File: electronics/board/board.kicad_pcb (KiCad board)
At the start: 2 copper layers, 141 x 30.5 mm, 80 parts, among them J1 Screw_Terminal_01x02, J10 Conn_01x02, J11 Conn_01x02, J12 Conn_01x02, J13 Conn_01x02, J14 Conn_01x02, J15 Conn_01x02, J16 Conn_01x02, J17 Conn_01x02, J18 Conn_01x02, J19 Conn_01x02, J2 Screw_Terminal_01x02, J20 Conn_01x02, J21 Conn_01x02, J22 Conn_01x02, J25 Screw_Terminal_01x01, J3 AVR-ISP-6, J4 USB_B_Micro, J5 Screw_Terminal_01x02, J6 Screw_Terminal_01x02, J7 Conn_01x02, J8 Conn_01x02, J9 Conn_01x02, Q1 IRF7404, SW1 SW_Push_Open_Dual, U1 LMV358, U2 ATmega32U4-AU, U3 NCP1117-5.0_TO252, U4 ST485EBDR, U5 ULN2803A, U6 ULN2803A, Y1 Crystal 16MHz

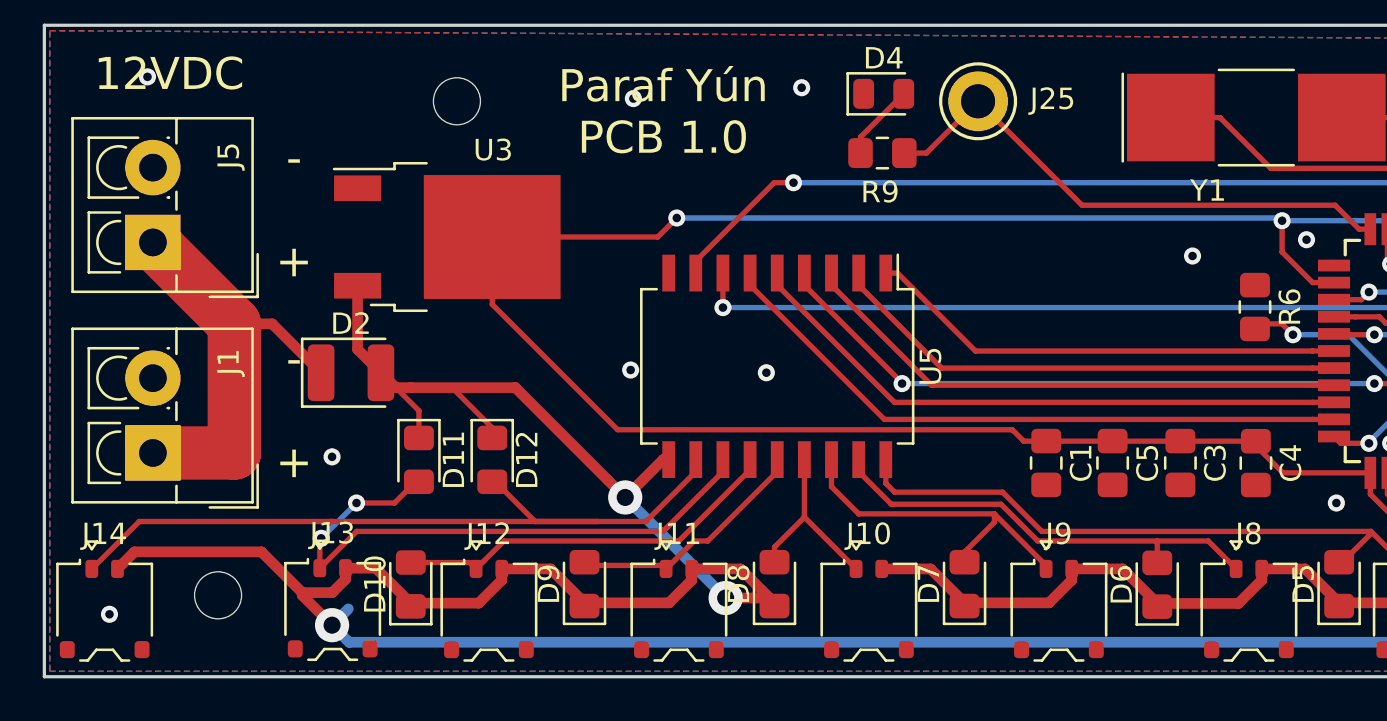
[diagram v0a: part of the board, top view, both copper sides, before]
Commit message: Diode protects only MCU
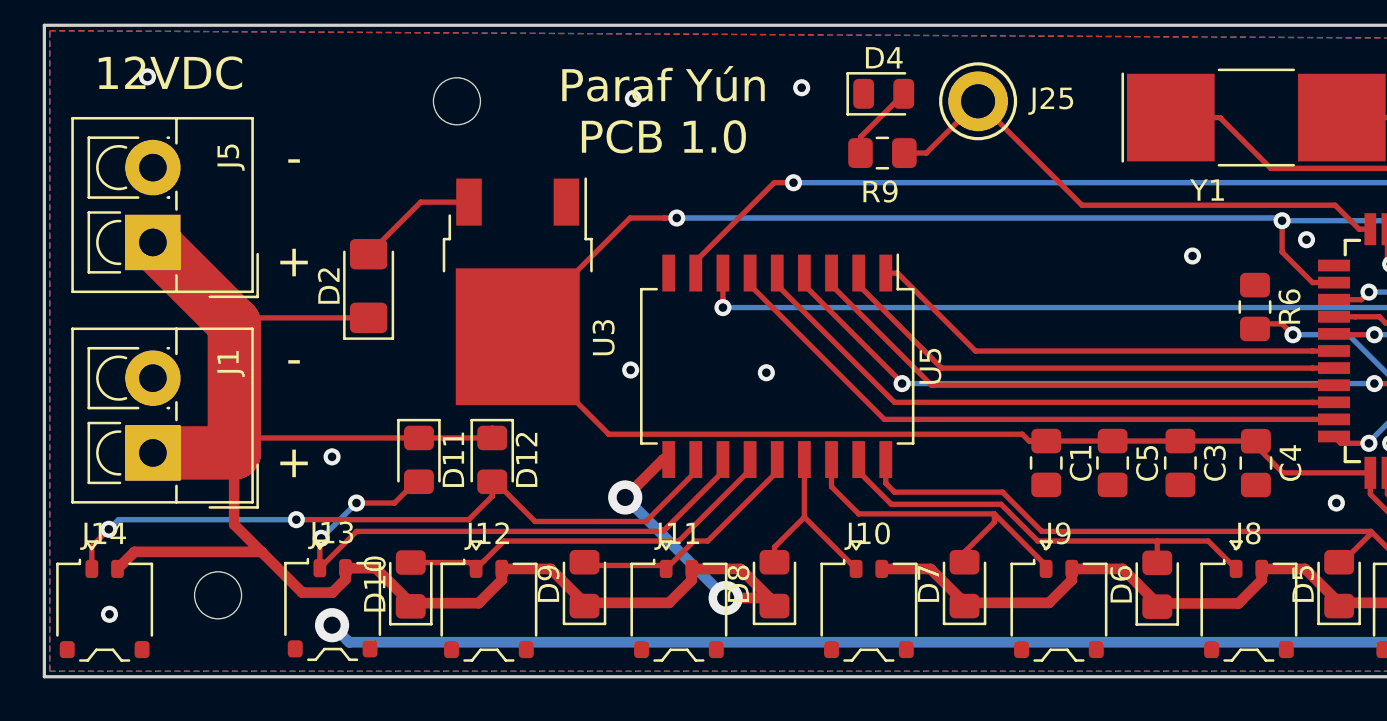
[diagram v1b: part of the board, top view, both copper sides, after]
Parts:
- D2: footprint Diode_SMD:D_1210_3225Metric -> Diode_SMD:D_1206_3216Metric_Pad1.42x1.75mm_HandSolder
- moved U3 4.18 mm to (86.9, 153.4), turned to 270 degrees
- moved D2 4.14 mm to (79.9, 153.2), turned to 90 degrees
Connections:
- D2 pad 1: Net-(D2-Pad1) -> +12V
- D2 pad 2: +12V -> Net-(D2-Pad2)
- J1 pad 1: Net-(D2-Pad1) -> +12V
- J5 pad 1: Net-(D2-Pad1) -> +12V
- U3 pad 3: +12V -> Net-(D2-Pad2)
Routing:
- net Net-(D2-Pad1): track 20.2 -> 0.00 mm
- net +12V: track 354.3 -> 363.3 mm
- net Net-(D2-Pad2): track 0.00 -> 5.71 mm
- net +5V: track 253.7 -> 249.8 mm
- net Net-(D12-Pad2): track 36.8 -> 33.5 mm, vias 0 -> 2

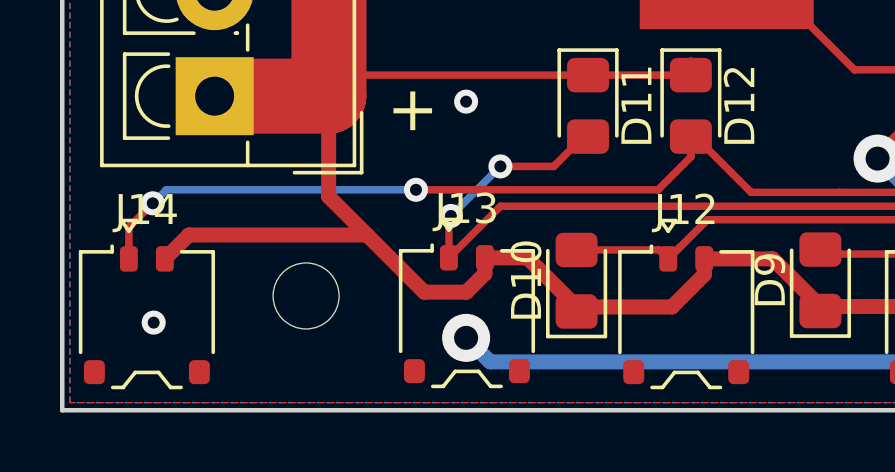
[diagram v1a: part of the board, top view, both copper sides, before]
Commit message: Bugfixes R 10k and 12v track
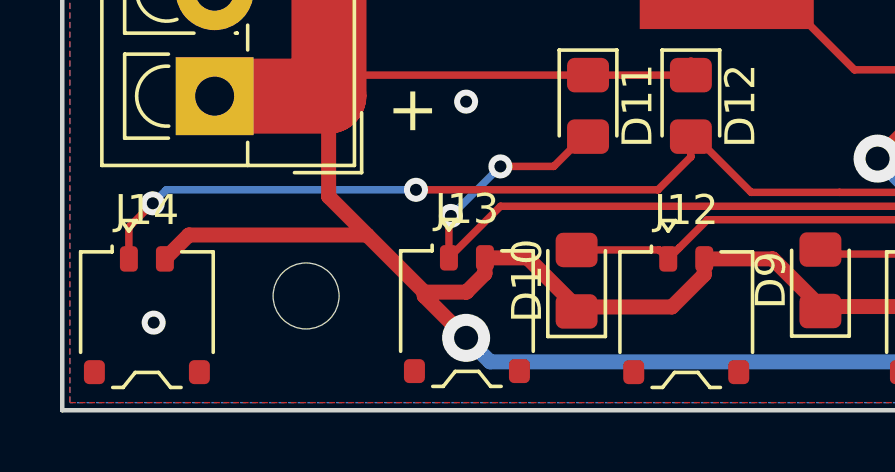
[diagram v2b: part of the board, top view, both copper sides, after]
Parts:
- R1, R2: value 10K -> 10k
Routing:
- net +12V: track 363.3 -> 365.4 mm
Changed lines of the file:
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@@
     (thickness 1.6)
     (drawings 23)
-    (tracks 757)
+    (tracks 759)
     (zones 0)
     (modules 80)
@@
   )
   (setup
-    (last_trace_width 0.25)
+    (last_trace_width 0.5)
     (user_trace_width 0.5)
     (user_trace_width 2.5)
@@
       (effects (font (size 1 1) (thickness 0.15)))
     )
-    (fp_text value 10K (at 0 1.65 180) (layer F.Fab)
+    (fp_text value 10k (at 0 1.65 180) (layer F.Fab)
       (effects (font (size 1 1) (thickness 0.15)))
     )
@@
       (effects (font (size 1 1) (thickness 0.15)))
     )
-    (fp_text value 10K (at 0 1.65 180) (layer F.Fab)
+    (fp_text value 10k (at 0 1.65 180) (layer F.Fab)
       (effects (font (size 1 1) (thickness 0.15)))
     )
@@
   (segment (start 73.94194 154.65806) (end 79.94142 154.65806) (width 0.25) (layer F.Cu) (net 8))
   (segment (start 73.66 154.94) (end 73.94194 154.65806) (width 0.25) (layer F.Cu) (net 8))
+  (segment (start 76.835 167.64) (end 78.232 169.037) (width 0.5) (layer F.Cu) (net 8))
+  (segment (start 76.835 167.513) (end 76.835 167.64) (width 0.5) (layer F.Cu) (net 8))
   (segment (start 198.785 160.02) (end 202.087 163.322) (width 0.25) (layer F.Cu) (net 9))
   (segment (start 197.993 160.02) (end 198.785 160.02) (width 0.25) (layer F.Cu) (net 9))

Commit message: Board v1.1 (not routed)
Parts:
- removed F3: MSMF050 500mA, Fuse:Fuse_1812_4532Metric
- removed J25: Screw_Terminal_01x01, TestPoint:TestPoint_Keystone_5005-5009_Compact
- removed REF** (x5): MountingHole_2.2mm_M2, MountingHole:MountingHole_2.2mm_M2
- added C12: 100uF, Capacitor_SMD:CP_Elec_6.3x5.2, F.Cu at (27.6, -24.4)
- added C13: 10uF, Capacitor_SMD:C_0805_2012Metric_Pad1.15x1.40mm_HandSolder, F.Cu at (17.1, -26.3)
- added F1: MSMF050 500mA, Fuse:Fuse_1812_4532Metric, F.Cu at (184.7, -27.7)
- added J23: Conn_01x02, Custom JST XH:JST_XH_S2B-XH-A_1x02_P2.50mm_Horizontal, F.Cu at (102.9, -8.09)
- C10: value 10uF -> 12-22pF; footprint Capacitor_SMD:CP_Elec_6.3x5.2 -> Capacitor_SMD:C_0805_2012Metric_Pad1.15x1.40mm_HandSolder
- C11: value 100nF -> 12-22pF
- C8: value 12-22pF -> 10uF
- C9: value 12-22pF -> 100nF
- D2: value DIODE -> LED; footprint Diode_SMD:D_1206_3216Metric_Pad1.42x1.75mm_HandSolder -> LED_SMD:LED_0805_2012Metric
- D4: value LED -> DIODE; footprint LED_SMD:LED_0805_2012Metric -> Diode_SMD:D_1206_3216Metric_Pad1.42x1.75mm_HandSolder
- J10, J11, J12, J13, J14, J15, J16, J17, J18, J19, J20, J21, J22, J8, J9: footprint Connector_JST:JST_ACH_BBM02B-ACHSS-GAN-ETF_1x02-1MP_P1.20mm_Vertical -> Custom JST XH:JST_XH_S2B-XH-A_1x02_P2.50mm_Horizontal
- J5: value Screw_Terminal_01x02 -> PD1; footprint TerminalBlock_4Ucon:TerminalBlock_4Ucon_1x02_P3.50mm_Vertical -> TestPoint:TestPoint_Keystone_5005-5009_Compact
- J7: value Conn_01x02 -> Screw_Terminal_01x02; footprint Connector_JST:JST_ACH_BBM02B-ACHSS-GAN-ETF_1x02-1MP_P1.20mm_Vertical -> TerminalBlock_4Ucon:TerminalBlock_4Ucon_1x02_P3.50mm_Vertical
- R6: value 10k -> 1k
- R7: value 1k -> 10k
- R8: value 1250 -> 1k
- R9: value 1k -> 1250
- moved J15 265.2 mm to (4.15, -8.09)
- moved J6 258.6 mm to (6.66, -35.5)
- moved D3 242.5 mm to (49.7, -24.6), turned to 90 degrees
- moved J7 219.7 mm to (47.0, -35.5)
- moved J2 217.4 mm to (60.8, -35.5)
- moved C2 210.9 mm to (72.2, -34.6)
- moved R6 210.0 mm to (4.81, -20.5), turned to 0 degrees
- moved R2 208.1 mm to (72.2, -29.3)
- moved R1 205.7 mm to (72.2, -24.0), turned to 0 degrees
- moved R8 205.2 mm to (55.7, -24.5), turned to 270 degrees
- moved C11 204.6 mm to (131.9, -38.2)
- moved U1 204.0 mm to (79.6, -31.4), turned to 270 degrees
- moved J1 202.6 mm to (20.1, -35.5), turned to 0 degrees
- moved C5 202.2 mm to (146.8, -38.2), turned to 180 degrees
- moved C7 199.7 mm to (169.9, -36.6), turned to 270 degrees
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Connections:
- C10 pad 1: VBUS -> GND
- C10 pad 2: GND -> Net-(C10-Pad2)
- C11 pad 1: VBUS -> GND
- C11 pad 2: GND -> Net-(C11-Pad2)
- C8 pad 1: GND -> VBUS
- C8 pad 2: Net-(C8-Pad2) -> GND
- C9 pad 1: GND -> VBUS
- C9 pad 2: Net-(C9-Pad2) -> GND
- D2 pad 1: +12V -> GND
- D4 pad 1: GND -> +12V
- J10 pad 1: Net-(D8-Pad2) -> Net-(D7-Pad2)
- J11 pad 1: Net-(D9-Pad2) -> Net-(D8-Pad2)
- J12 pad 1: Net-(D10-Pad2) -> Net-(D9-Pad2)
- J13 pad 1: Net-(D11-Pad2) -> Net-(D10-Pad2)
- J14 pad 1: Net-(D12-Pad2) -> Net-(D11-Pad2)
- J15 pad 1: Net-(D13-Pad2) -> Net-(D12-Pad2)
- J16 pad 1: Net-(D14-Pad2) -> Net-(D13-Pad2)
- J17 pad 1: Net-(D15-Pad2) -> Net-(D14-Pad2)
- J18 pad 1: Net-(D16-Pad2) -> Net-(D15-Pad2)
- J19 pad 1: Net-(D17-Pad2) -> Net-(D16-Pad2)
- J20 pad 1: Net-(D18-Pad2) -> Net-(D17-Pad2)
- J21 pad 1: Net-(D19-Pad2) -> Net-(D18-Pad2)
- J22 pad 1: Net-(D20-Pad2) -> Net-(D19-Pad2)
- J5 pad 1: +12V -> Net-(J5-Pad1)
- J6 pad 1: Net-(J2-Pad1) -> +12V
- J6 pad 2: Net-(J2-Pad2) -> GND
- J7 pad 1: Net-(D5-Pad2) -> Net-(J2-Pad1)
- J7 pad 2: +12V -> Net-(J2-Pad2)
- J8 pad 1: Net-(D6-Pad2) -> Net-(D5-Pad2)
- J9 pad 1: Net-(D7-Pad2) -> Net-(D6-Pad2)
- R6 pad 1: GND -> Net-(D2-Pad2)
- R6 pad 2: Net-(R6-Pad2) -> +5V
- R7 pad 1: Net-(D3-Pad2) -> GND
- R7 pad 2: +5V -> Net-(R7-Pad2)
- R8 pad 1: Net-(R8-Pad1) -> Net-(D3-Pad2)
- R8 pad 2: Net-(R8-Pad2) -> Net-(J5-Pad1)
- R9 pad 1: Net-(D4-Pad2) -> Net-(R9-Pad1)
- R9 pad 2: Net-(J25-Pad1) -> Net-(R9-Pad2)
- U2 pad 16: Net-(C9-Pad2) -> Net-(C11-Pad2)
- U2 pad 17: Net-(C8-Pad2) -> Net-(C10-Pad2)
- U2 pad 19: Net-(U2-Pad19) -> Net-(J5-Pad1)
- U2 pad 22: Net-(J25-Pad1) -> Net-(U2-Pad22)
- U2 pad 25: Net-(R8-Pad1) -> Net-(R9-Pad1)
- U2 pad 33: Net-(R6-Pad2) -> Net-(R7-Pad2)
- U3 pad 3: Net-(D2-Pad2) -> Net-(D4-Pad2)
- U4 pad 2: Net-(R8-Pad2) -> Net-(R9-Pad2)
- U4 pad 3: Net-(R8-Pad2) -> Net-(R9-Pad2)
- U5 pad 1: Net-(U2-Pad28) -> Net-(U2-Pad32)
- U5 pad 2: Net-(U2-Pad29) -> Net-(U2-Pad31)
- U5 pad 4: Net-(U2-Pad12) -> Net-(U2-Pad29)
- U5 pad 5: Net-(U2-Pad31) -> Net-(U2-Pad28)
- U5 pad 6: Net-(U2-Pad32) -> Net-(U2-Pad27)
- U5 pad 7: Net-(U2-Pad18) -> Net-(U2-Pad26)
- U5 pad 8: Net-(U2-Pad19) -> Net-(U2-Pad22)
- U6 pad 1: Net-(U2-Pad26) -> Net-(U2-Pad18)
- U6 pad 2: Net-(U2-Pad27) -> Net-(U2-Pad12)
- Y1 pad 1: Net-(C8-Pad2) -> Net-(C10-Pad2)
- Y1 pad 2: Net-(C9-Pad2) -> Net-(C11-Pad2)
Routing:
- net +12V: track 365.4 -> 0.00 mm, vias 7 -> 0
- net +5V: track 249.8 -> 0.00 mm, vias 7 -> 0
- net /RESET: track 94.1 -> 0.00 mm, vias 3 -> 0
- net Net-(F1-Pad2): track 67.8 -> 0.00 mm, vias 2 -> 0
- net VBUS: track 65.7 -> 0.00 mm, vias 3 -> 0
- net Net-(R4-Pad1): track 65.4 -> 0.00 mm, vias 4 -> 0
- net Net-(R5-Pad1): track 55.9 -> 0.00 mm, vias 2 -> 0
- net Net-(U2-Pad26): track 54.3 -> 0.00 mm, vias 2 -> 0
- net Net-(U2-Pad27): track 52.0 -> 0.00 mm, vias 2 -> 0
- net GND: track 49.4 -> 0.00 mm, vias 22 -> 0
- net Net-(U2-Pad41): track 45.2 -> 0.00 mm, vias 2 -> 0
- net Net-(U2-Pad40): track 44.9 -> 0.00 mm, vias 2 -> 0
- net Net-(U2-Pad39): track 44.5 -> 0.00 mm, vias 2 -> 0
- net Net-(U2-Pad37): track 44.4 -> 0.00 mm, vias 2 -> 0
- net Net-(U2-Pad38): track 44.4 -> 0.00 mm, vias 2 -> 0
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- removed copper zone on B.Cu, net GND
- removed copper zone on F.Cu, net GND
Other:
- board outline removed
- board text removed: "- +"
- board text removed: "12VDC"
- board text removed: "1:MISO 2:5V 3:SCK 4:MOSI"
- board text removed: "A+ B-"
- board text removed: "AVR ISP↘"
- board text removed: "B- A+"
- board text removed: "PWR LED"
- board text removed: "Paraf Yún PCB 1.0"
- board text removed: "Paraf Yún PCB 1.0 Yoan Mollard"
- board text removed: "RESET"
- board text removed: "RS485"
- board text removed: "RS485→"

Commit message: Routed 1.1
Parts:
- moved U6 40.5 mm to (161.6, -19.6), turned to 270 degrees
- moved D2 37.1 mm to (34.8, -37.1), turned to 90 degrees
- moved R6 30.2 mm to (30.0, -37.0), turned to 270 degrees
- moved R9 23.9 mm to (72.8, -34.7), turned to 90 degrees
- moved J5 23.9 mm to (40.3, -19.1)
- moved R1 22.5 mm to (50.1, -19.9)
- moved C12 20.6 mm to (6.99, -23.5), turned to 270 degrees
- moved C2 18.0 mm to (57.7, -23.9)
- moved R2 17.4 mm to (57.7, -19.8)
- moved R5 12.8 mm to (172.8, -18.0)
- moved RV2 12.1 mm to (179.1, -18.1)
- moved D12 12.0 mm to (15.2, -16.5), turned to 0 degrees
- moved U3 11.6 mm to (27.3, -22.9)
- moved C6 10.9 mm to (69.1, -21.9), turned to 90 degrees
- moved C10 10.3 mm to (130.3, -33.5), turned to 90 degrees
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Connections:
- U5 pad 1: Net-(U2-Pad32) -> Net-(U2-Pad26)
- U5 pad 2: Net-(U2-Pad31) -> Net-(U2-Pad27)
- U5 pad 3: Net-(U2-Pad30) -> Net-(U2-Pad28)
- U5 pad 5: Net-(U2-Pad28) -> Net-(U2-Pad30)
- U5 pad 6: Net-(U2-Pad27) -> Net-(U2-Pad31)
- U5 pad 7: Net-(U2-Pad26) -> Net-(U2-Pad32)
- U6 pad 1: Net-(U2-Pad18) -> Net-(U2-Pad12)
- U6 pad 2: Net-(U2-Pad12) -> Net-(U2-Pad18)
- U6 pad 3: Net-(U2-Pad41) -> Net-(U2-Pad36)
- U6 pad 4: Net-(U2-Pad40) -> Net-(U2-Pad37)
- U6 pad 5: Net-(U2-Pad39) -> Net-(U2-Pad38)
- U6 pad 6: Net-(U2-Pad38) -> Net-(U2-Pad39)
- U6 pad 7: Net-(U2-Pad37) -> Net-(U2-Pad40)
- U6 pad 8: Net-(U2-Pad36) -> Net-(U2-Pad41)
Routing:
- net +12V: track 0.00 -> 781.3 mm, vias 0 -> 8
- net +5V: track 0.00 -> 412.8 mm, vias 0 -> 2
- net VBUS: track 0.00 -> 117.1 mm, vias 0 -> 2
- net Net-(J5-Pad1): track 0.00 -> 115.6 mm, vias 0 -> 2
- net Net-(D12-Pad2): track 0.00 -> 106.3 mm
- net Net-(D11-Pad2): track 0.00 -> 94.2 mm
- net Net-(D10-Pad2): track 0.00 -> 82.5 mm
- net /RESET: track 0.00 -> 77.1 mm, vias 0 -> 2
- net Net-(D9-Pad2): track 0.00 -> 71.4 mm
- net Net-(R9-Pad1): track 0.00 -> 68.3 mm, vias 0 -> 2
- net Net-(U2-Pad21): track 0.00 -> 67.5 mm, vias 0 -> 2
- net Net-(U2-Pad20): track 0.00 -> 63.2 mm, vias 0 -> 2
- net Net-(D20-Pad2): track 0.00 -> 63.0 mm
- net Net-(D8-Pad2): track 0.00 -> 60.2 mm
- net Net-(D19-Pad2): track 0.00 -> 52.1 mm
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- added copper zone on B.Cu, net GND
- added copper zone on F.Cu, net GND

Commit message: PCB layout
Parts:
- added REF**: MountingHole_2.5mm, MountingHole:MountingHole_2.5mm, F.Cu at (107.5, 25.7)
- added REF**: MountingHole_2.2mm_M2, MountingHole:MountingHole_2.2mm_M2, F.Cu at (7.49, 25.5)
- added REF**: MountingHole_2.2mm_M2, MountingHole:MountingHole_2.2mm_M2, F.Cu at (187.9, 25.5)
- added REF**: MountingHole_2.2mm_M2, MountingHole:MountingHole_2.2mm_M2, F.Cu at (72.1, 5.54)
- added REF**: MountingHole_2.2mm_M2, MountingHole:MountingHole_2.2mm_M2, F.Cu at (169.0, 4.16)
- moved D12 43.9 mm to (16.3, 27.3)
- moved Y1 41.3 mm to (117.4, 6.31)
- moved R9 41.0 mm to (76.1, 6.17)
- moved C7 41.0 mm to (173.9, 4.21)
- moved D1 40.8 mm to (178.7, 4.11)
- moved C1 40.7 mm to (134.2, 19.8)
- moved C11 40.7 mm to (126.8, 7.22)
- moved C12 40.7 mm to (8.00, 17.2)
- moved C13 40.7 mm to (16.4, 15.4)
- moved C2 40.7 mm to (58.7, 16.9)
- moved C4 40.7 mm to (139.4, 23.2)
- moved C6 40.7 mm to (70.1, 18.8)
- moved C8 40.7 mm to (173.8, 10.7)
- moved D10 40.7 mm to (25.6, 32.1)
- moved D11 40.7 mm to (12.8, 32.1)
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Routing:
- net Net-(C11-Pad2): track 25.7 -> 40.7 mm
- net Net-(D4-Pad2): track 17.4 -> 6.59 mm
- net +5V: track 412.8 -> 415.9 mm
- net Net-(R9-Pad2): track 17.4 -> 14.9 mm
- net Net-(R9-Pad1): track 68.3 -> 65.9 mm
- net Net-(D12-Pad2): track 106.3 -> 104.3 mm
- net Net-(C10-Pad2): track 30.8 -> 32.4 mm
- net /RESET: track 77.1 -> 76.1 mm
- net Net-(J5-Pad1): vias 2 -> 3
- net GND: vias 64 -> 70
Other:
- board text added: "+ -"
- board text added: "12V"
- board text added: "A+ B-"
- board text added: "PARAF board v1.1 Yoan Mollard"
- board text added: "PD1"
- board text added: "POWER LED"
- board text added: "RS485"

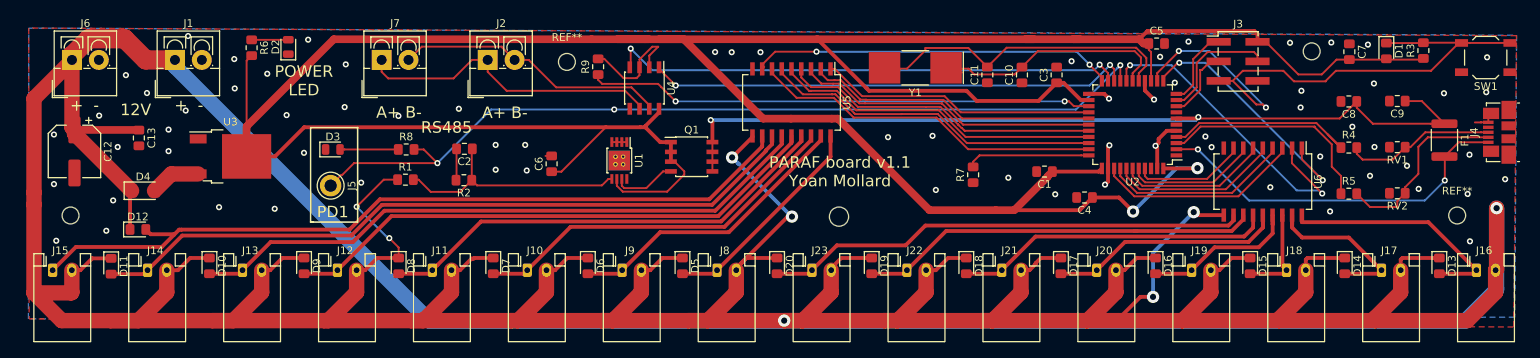
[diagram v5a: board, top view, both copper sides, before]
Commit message: cut layer + refilled zones
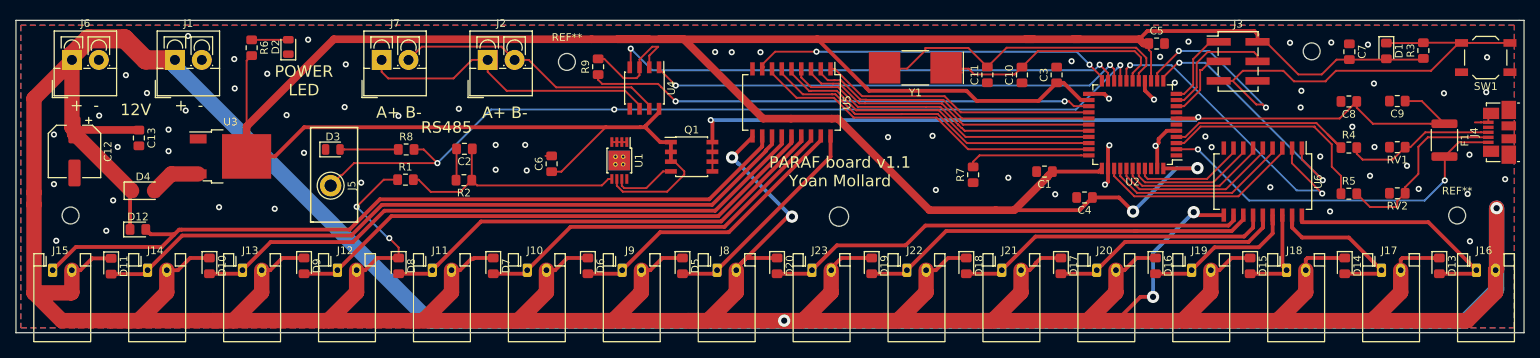
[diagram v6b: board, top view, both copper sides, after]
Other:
- board outline added: 196.2 x 40.6 mm
- board text removed: "PD1"
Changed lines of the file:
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@@
   (general
     (thickness 1.6)
-    (drawings 15)
+    (drawings 19)
     (tracks 842)
     (zones 0)
@@
   )
   (setup
-    (last_trace_width 0.5)
+    (last_trace_width 0.25)
     (user_trace_width 0.5)
     (user_trace_width 1)
@@
     (pad 1 np_thru_hole circle (at 0 0) (size 2.2 2.2) (drill 2.2) (layers *.Cu *.Mask))
   )
-  (gr_text PD1 (at 41.6 25.06) (layer F.SilkS)
-    (effects (font (size 1.5 1.5) (thickness 0.3)))
-  )
+  (gr_line (start 196.6 40.775) (end 0.385 40.775) (layer Edge.Cuts) (width 0.15))
+  (gr_line (start 196.6 0.135) (end 196.6 40.775) (layer Edge.Cuts) (width 0.15))
+  (gr_line (start 195.965 0.135) (end 196.6 0.135) (layer Edge.Cuts) (width 0.15))
+  (gr_line (start 0.385 0.135) (end 195.965 0.135) (layer Edge.Cuts) (width 0.15))
+  (gr_line (start 0.385 40.775) (end 0.385 0.135) (layer Edge.Cuts) (width 0.15))
   (gr_line (start 38.72 26.4) (end 39.04 26.38) (layer F.SilkS) (width 0.2))
   (gr_line (start 38.72 26.31) (end 38.72 26.4) (layer F.SilkS) (width 0.2))
@@
     (polygon
       (pts
-        (xy 195.27 40.03) (xy 195.62 2.13) (xy 2.05 1.13) (xy 2.1 38.98)
+        (xy 195.33 40.14) (xy 195.33 0.77) (xy 1.02 0.77) (xy 1.02 40.14)
       )
     )
@@
     (polygon
       (pts
-        (xy 195.63 2.07) (xy 195.39 38.76) (xy 2 38.98) (xy 2.05 1.14)
+        (xy 1.02 0.77) (xy 1.02 40.14) (xy 195.33 40.14) (xy 195.33 0.77)
       )
     )
